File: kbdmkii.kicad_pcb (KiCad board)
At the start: 2 copper layers, 132.3 x 81.7 mm, 58 parts, among them SW1 SW_Push, SW10 SW_Push, SW11 SW_Push, SW12 SW_Push, SW13 SW_Push, SW14 SW_Push, SW15 SW_Push, SW16 SW_Push, SW17 SW_Push, SW18 SW_Push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

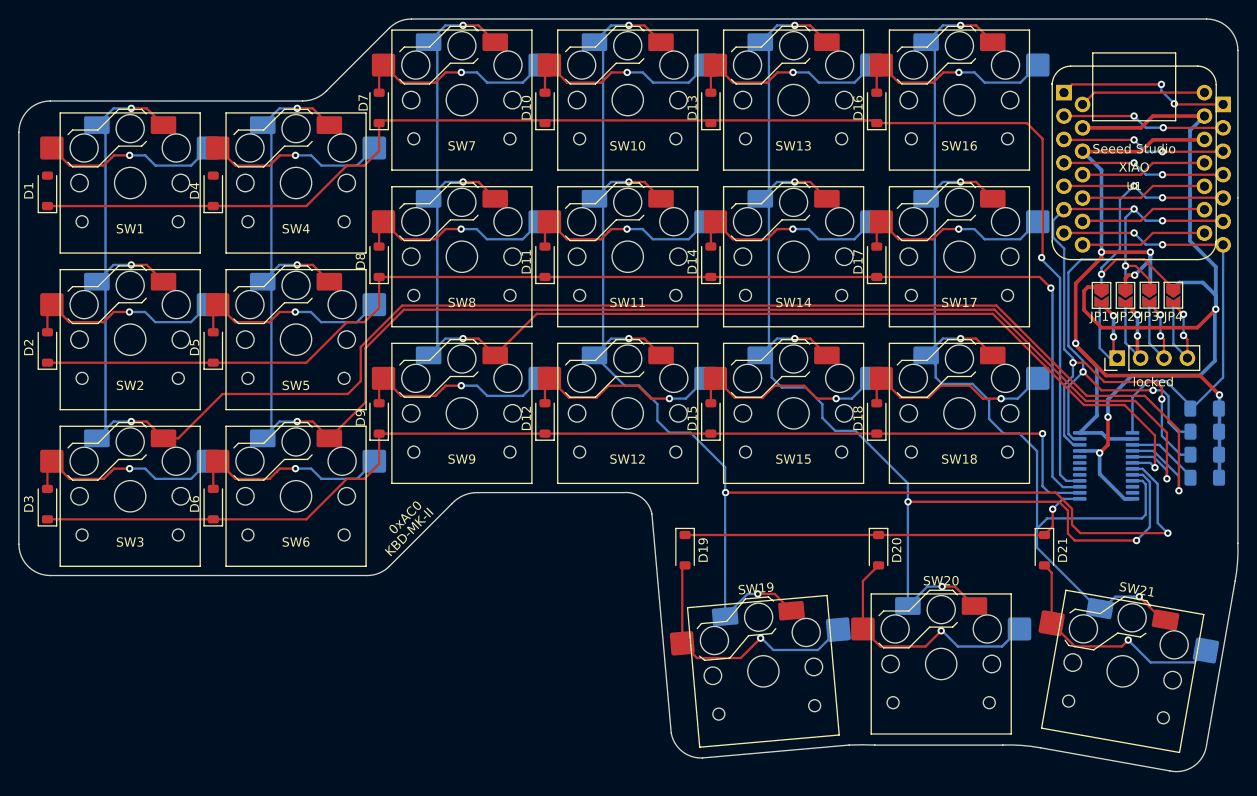
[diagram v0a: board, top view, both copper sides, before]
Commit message: add ground plane
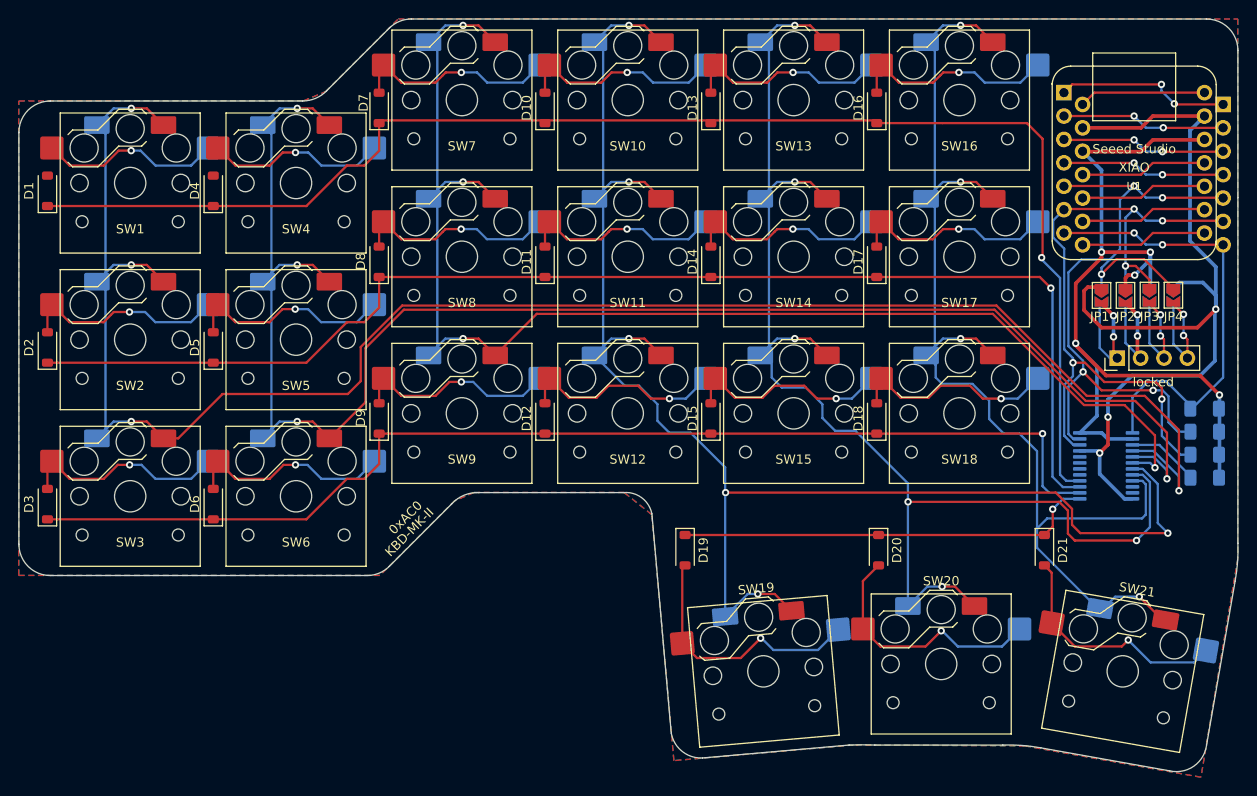
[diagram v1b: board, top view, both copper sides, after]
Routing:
- added copper zone on B.Cu, net GND
- added copper zone on F.Cu, net GND

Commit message: improved ground plane, fixed some warnings
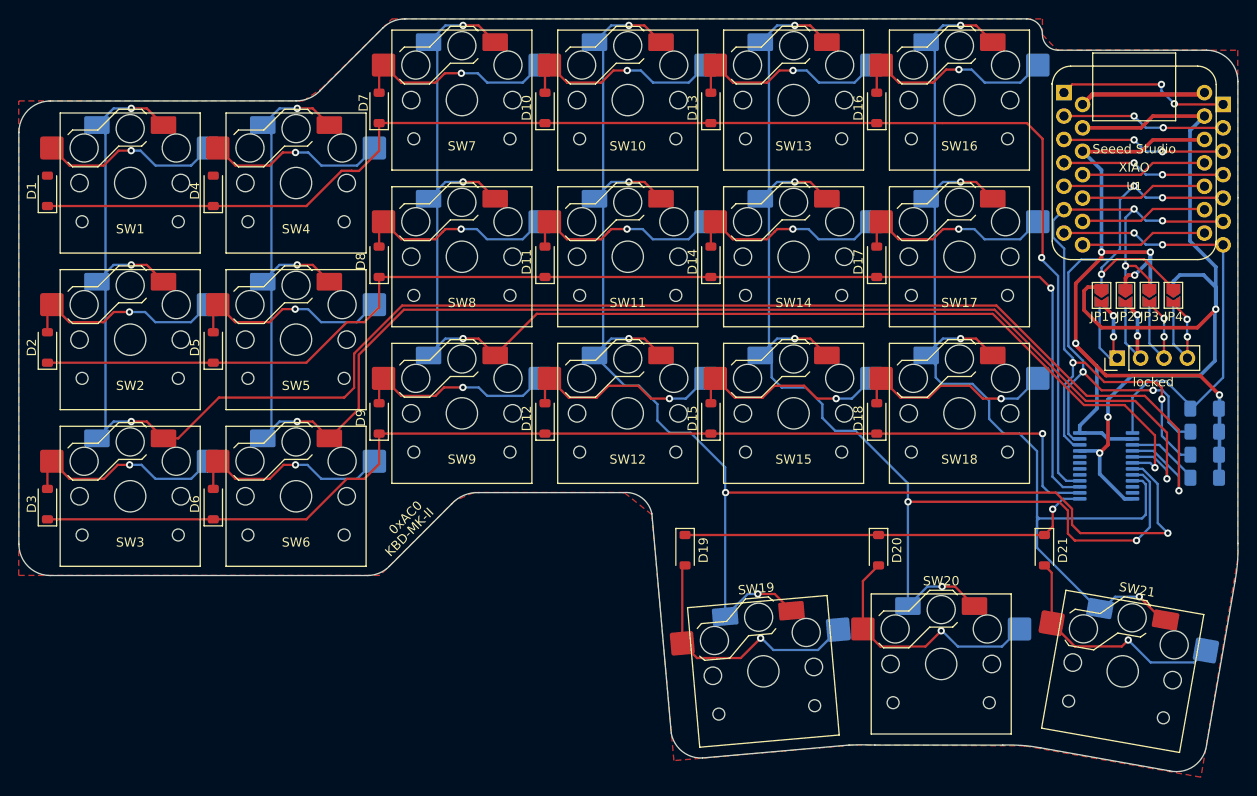
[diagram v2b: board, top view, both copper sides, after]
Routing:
- net GND: track 97.8 -> 99.5 mm
- net /COL 5: track 126.2 -> 127.1 mm
- removed copper zone on B.Cu, net GND
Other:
- outline, holes or cut-outs redrawn
